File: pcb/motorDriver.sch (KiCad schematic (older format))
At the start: 5 parts, among them U5 VNH7070AS

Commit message: first version of the new feature set
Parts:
- removed R7, R8, R9: 1k, Resistor_SMD:R_0805_2012Metric_Pad1.15x1.40mm_HandSolder, symbol Device:R
- added C13: 560u, Capacitor_SMD:CP_Elec_10x10.5, symbol Device:CP
- C12: renamed from C13; footprint Capacitor_SMD:C_0805_2012Metric_Pad1.15x1.40mm_HandSolder -> Capacitor_SMD:C_0805_2012Metric
- renumbered U5 to U3
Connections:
- net +12V: now also C13.1
- net GND: now also C13.2
- net INA: now also U3.3 (INA)
- net InB: now also U3.6 (INB)
- net PWM: now also U3.11 (PWM)
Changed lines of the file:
@@
 $Descr A4 11693 8268
 encoding utf-8
-Sheet 4 7
+Sheet 3 17
 Title "H-Bridge Motor Driver"
 Date ""
@@
 PWM
 $Comp
-L Driver_Motor_own:VNH7070AS U5
+L Driver_Motor_own:VNH7070AS U3
 U 1 1 5C445805
 P 3300 1350
-AR Path="/5C443F4F/5C445805" Ref="U5"  Part="1"
-AR Path="/5C443F5E/5C445805" Ref="U6"  Part="1"
-F 0 "U6" H 3300 1666 50  0000 C CNN
+AR Path="/5C443F4F/5C445805" Ref="U3"  Part="1"
+AR Path="/5C443F5E/5C445805" Ref="U?"  Part="1"
+AR Path="/5C9CCBB2/5C445805" Ref="U5"  Part="1"
+AR Path="/5C9DA548/5C445805" Ref="U?"  Part="1"
+AR Path="/5C9DA551/5C445805" Ref="U9"  Part="1"
+F 0 "U3" H 3300 1666 50  0000 C CNN
 F 1 "VNH7070AS" H 3300 1575 50  0000 C CNN
 F 2 "Package_SO:SOIC-16_3.9x9.9mm_P1.27mm" H 3250 1400 50  0001 C CNN
@@
 	3500 2950 4150 2950
 $Comp
-L Device:C C13
+L Device:C C12
 U 1 1 5C44655B
 P 4150 900
-AR Path="/5C443F4F/5C44655B" Ref="C13"  Part="1"
-AR Path="/5C443F5E/5C44655B" Ref="C15"  Part="1"
-F 0 "C15" H 4265 946 50  0000 L CNN
+AR Path="/5C443F4F/5C44655B" Ref="C12"  Part="1"
+AR Path="/5C443F5E/5C44655B" Ref="C?"  Part="1"
+AR Path="/5C9CCBB2/5C44655B" Ref="C21"  Part="1"
+AR Path="/5C9DA548/5C44655B" Ref="C?"  Part="1"
+AR Path="/5C9DA551/5C44655B" Ref="C32"  Part="1"
+F 0 "C12" H 4265 946 50  0000 L CNN
 F 1 "100n" H 4265 855 50  0000 L CNN
-F 2 "Capacitor_SMD:C_0805_2012Metric_Pad1.15x1.40mm_HandSolder" H 4188 750 50  0001 C CNN
+F 2 "Capacitor_SMD:C_0805_2012Metric" H 4188 750 50  0001 C CNN
 F 3 "~" H 4150 900 50  0001 C CNN
 	1    4150 900
@@
 Wire Wire Line
 	3850 1650 5600 1650
-$Comp
-L Device:R R7
-U 1 1 5C446EC8
-P 1750 1450
-AR Path="/5C443F4F/5C446EC8" Ref="R7"  Part="1"
-AR Path="/5C443F5E/5C446EC8" Ref="R10"  Part="1"
-F 0 "R10" V 1543 1450 50  0000 C CNN
-F 1 "1k" V 1634 1450 50  0000 C CNN
-F 2 "Resistor_SMD:R_0805_2012Metric_Pad1.15x1.40mm_HandSolder" V 1680 1450 50  0001 C CNN
-F 3 "~" H 1750 1450 50  0001 C CNN
-	1    1750 1450
-	0    1    1    0
-$EndComp
-$Comp
-L Device:R R8
-U 1 1 5C446F11
-P 1750 1750
-AR Path="/5C443F4F/5C446F11" Ref="R8"  Part="1"
-AR Path="/5C443F5E/5C446F11" Ref="R11"  Part="1"
-F 0 "R11" V 1543 1750 50  0000 C CNN
-F 1 "1k" V 1634 1750 50  0000 C CNN
-F 2 "Resistor_SMD:R_0805_2012Metric_Pad1.15x1.40mm_HandSolder" V 1680 1750 50  0001 C CNN
-F 3 "~" H 1750 1750 50  0001 C CNN
-	1    1750 1750
-	0    1    1    0
-$EndComp
-$Comp
-L Device:R R9
-U 1 1 5C446F3B
-P 1750 2050
-AR Path="/5C443F4F/5C446F3B" Ref="R9"  Part="1"
-AR Path="/5C443F5E/5C446F3B" Ref="R12"  Part="1"
-F 0 "R12" V 1543 2050 50  0000 C CNN
-F 1 "1k" V 1634 2050 50  0000 C CNN
-F 2 "Resistor_SMD:R_0805_2012Metric_Pad1.15x1.40mm_HandSolder" V 1680 2050 50  0001 C CNN
-F 3 "~" H 1750 2050 50  0001 C CNN
-	1    1750 2050
-	0    1    1    0
-$EndComp
-Wire Wire Line
-	850  1450 1600 1450
-Wire Wire Line
-	1900 1450 2750 1450
-Wire Wire Line
-	850  1750 1600 1750
 Wire Wire Line
 	1900 1750 1900 1550
@@
 	1900 1550 2750 1550
 Wire Wire Line
-	1900 2050 2250 2050
-Wire Wire Line
 	2250 2050 2250 1650
 Wire Wire Line
 	2250 1650 2750 1650
 Wire Wire Line
-	1600 2050 850  2050
-Wire Wire Line
-	4150 750  5600 750
+	4150 750  4950 750
 $Comp
-L power:GND #PWR0103
+L power:GND #PWR?
 U 1 1 5C60F6E8
 P 5600 2950
-AR Path="/5C443F5E/5C60F6E8" Ref="#PWR0103"  Part="1"
-AR Path="/5C443F4F/5C60F6E8" Ref="#PWR0101"  Part="1"
-F 0 "#PWR0103" H 5600 2700 50  0001 C CNN
+AR Path="/5C443F5E/5C60F6E8" Ref="#PWR?"  Part="1"
+AR Path="/5C443F4F/5C60F6E8" Ref="#PWR047"  Part="1"
+AR Path="/5C9CCBB2/5C60F6E8" Ref="#PWR049"  Part="1"
+AR Path="/5C9DA548/5C60F6E8" Ref="#PWR?"  Part="1"
+AR Path="/5C9DA551/5C60F6E8" Ref="#PWR051"  Part="1"
+F 0 "#PWR051" H 5600 2700 50  0001 C CNN
 F 1 "GND" H 5605 2777 50  0000 C CNN
 F 2 "" H 5600 2950 50  0001 C CNN
@@
 $EndComp
 $Comp
-L power:+12V #PWR0104
+L power:+12V #PWR?
 U 1 1 5C60F720
 P 5600 750
-AR Path="/5C443F5E/5C60F720" Ref="#PWR0104"  Part="1"
-AR Path="/5C443F4F/5C60F720" Ref="#PWR0102"  Part="1"
-F 0 "#PWR0104" H 5600 600 50  0001 C CNN
+AR Path="/5C443F5E/5C60F720" Ref="#PWR?"  Part="1"
+AR Path="/5C443F4F/5C60F720" Ref="#PWR046"  Part="1"
+AR Path="/5C9CCBB2/5C60F720" Ref="#PWR048"  Part="1"
+AR Path="/5C9DA548/5C60F720" Ref="#PWR?"  Part="1"
+AR Path="/5C9DA551/5C60F720" Ref="#PWR050"  Part="1"
+F 0 "#PWR050" H 5600 600 50  0001 C CNN
 F 1 "+12V" H 5615 923 50  0000 C CNN
 F 2 "" H 5600 750 50  0001 C CNN
@@
 	1    0    0    -1
 $EndComp
+Wire Wire Line
+	850  1450 2750 1450
+Wire Wire Line
+	850  1750 1900 1750
+Wire Wire Line
+	850  2050 2250 2050
+$Comp
+L Device:CP C13
+U 1 1 5C9C254B
+P 4950 900
+AR Path="/5C443F4F/5C9C254B" Ref="C13"  Part="1"
+AR Path="/5C9CCBB2/5C9C254B" Ref="C22"  Part="1"
+AR Path="/5C9DA548/5C9C254B" Ref="C?"  Part="1"
+AR Path="/5C9DA551/5C9C254B" Ref="C33"  Part="1"
+F 0 "C13" H 5068 946 50  0000 L CNN
+F 1 "560u" H 5068 855 50  0000 L CNN
+F 2 "Capacitor_SMD:CP_Elec_10x10.5" H 4988 750 50  0001 C CNN
+F 3 "~" H 4950 900 50  0001 C CNN
+	1    4950 900
+	1    0    0    -1
+$EndComp
+Connection ~ 4950 750
+Wire Wire Line
+	4950 750  5600 750
+Wire Wire Line
+	4950 1050 4150 1050
+Connection ~ 4150 1050
 $EndSCHEMATC

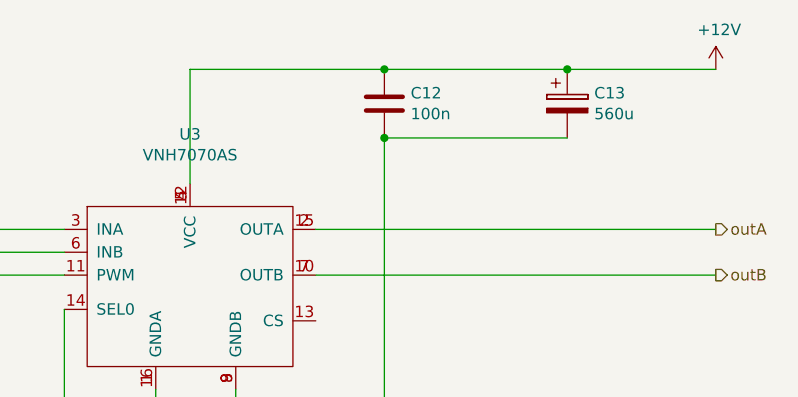
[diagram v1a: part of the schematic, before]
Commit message: Added an other uart for ardusimple RTK2Bligh daughterboard on top of the normal RTK2B. Removed two LEDs to free up PINs
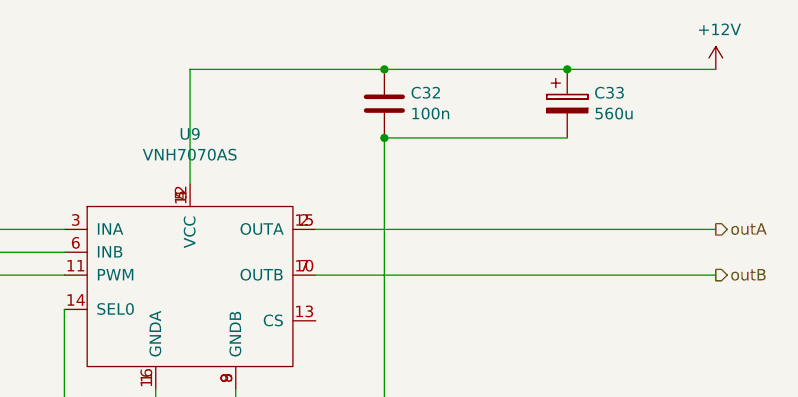
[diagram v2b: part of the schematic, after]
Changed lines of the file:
@@
 AR Path="/5C9DA548/5C445805" Ref="U?"  Part="1"
 AR Path="/5C9DA551/5C445805" Ref="U9"  Part="1"
-F 0 "U3" H 3300 1666 50  0000 C CNN
+F 0 "U9" H 3300 1666 50  0000 C CNN
 F 1 "VNH7070AS" H 3300 1575 50  0000 C CNN
 F 2 "Package_SO:SOIC-16_3.9x9.9mm_P1.27mm" H 3250 1400 50  0001 C CNN
@@
 AR Path="/5C9DA548/5C44655B" Ref="C?"  Part="1"
 AR Path="/5C9DA551/5C44655B" Ref="C32"  Part="1"
-F 0 "C12" H 4265 946 50  0000 L CNN
+F 0 "C32" H 4265 946 50  0000 L CNN
 F 1 "100n" H 4265 855 50  0000 L CNN
 F 2 "Capacitor_SMD:C_0805_2012Metric" H 4188 750 50  0001 C CNN
@@
 AR Path="/5C9DA548/5C9C254B" Ref="C?"  Part="1"
 AR Path="/5C9DA551/5C9C254B" Ref="C33"  Part="1"
-F 0 "C13" H 5068 946 50  0000 L CNN
+F 0 "C33" H 5068 946 50  0000 L CNN
 F 1 "560u" H 5068 855 50  0000 L CNN
 F 2 "Capacitor_SMD:CP_Elec_10x10.5" H 4988 750 50  0001 C CNN
